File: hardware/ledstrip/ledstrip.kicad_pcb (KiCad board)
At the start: 4 copper layers, 107 x 107.5 mm, 126 parts, among them J1 Conn_ARM_JTAG_SWD_10, J2 USB_C_Receptacle_USB2.0_16P, J4 BMS connectors, J5 Ledstrip connector, J6 Header for STUSB4500 I2C, Q1 Q_NMOS, Q10 Q_PMOS, Q11 Q_NMOS, Q2 Q_NMOS, Q3 Q_NMOS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

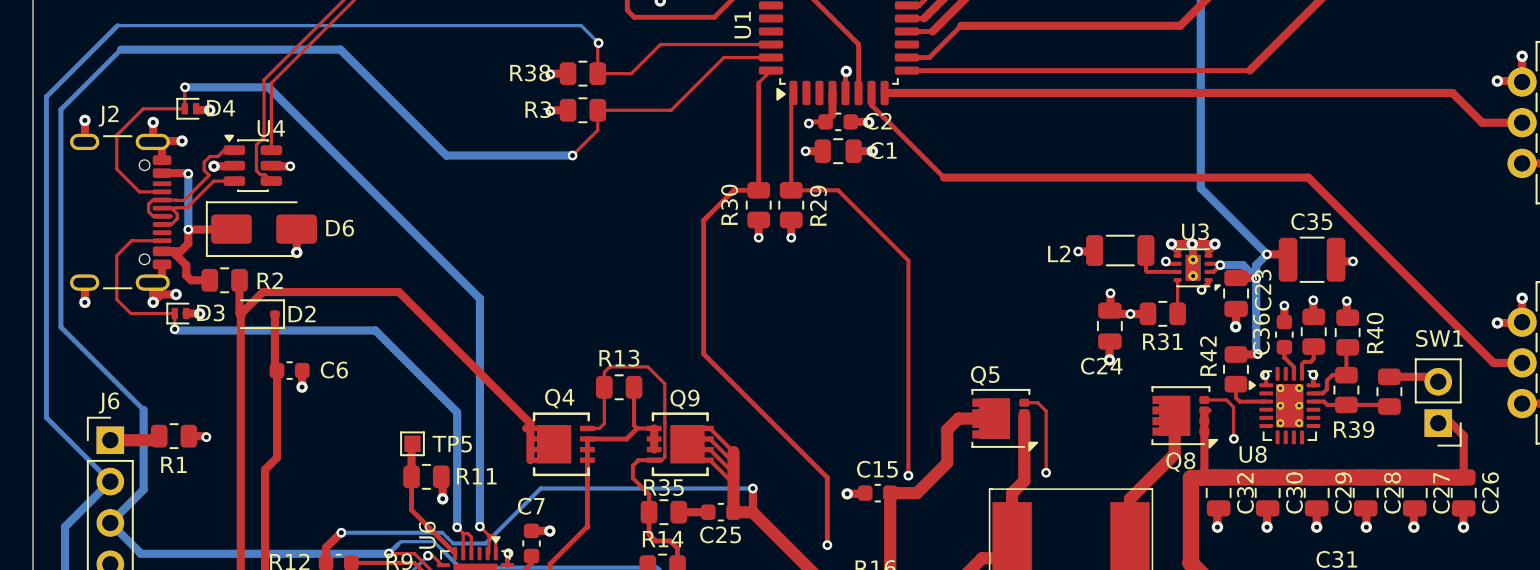
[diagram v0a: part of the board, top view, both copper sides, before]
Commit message: Fix ERC and DRC errors.
Use a custom copy of USB-C in project library to avoid having a version
mismatch with CI.
Fix QFN-20-1EP_3x4mm_P0.5mm_EP1.65x2.65mm_ThermalVias  mismatch pins.
Fix ERC errors.
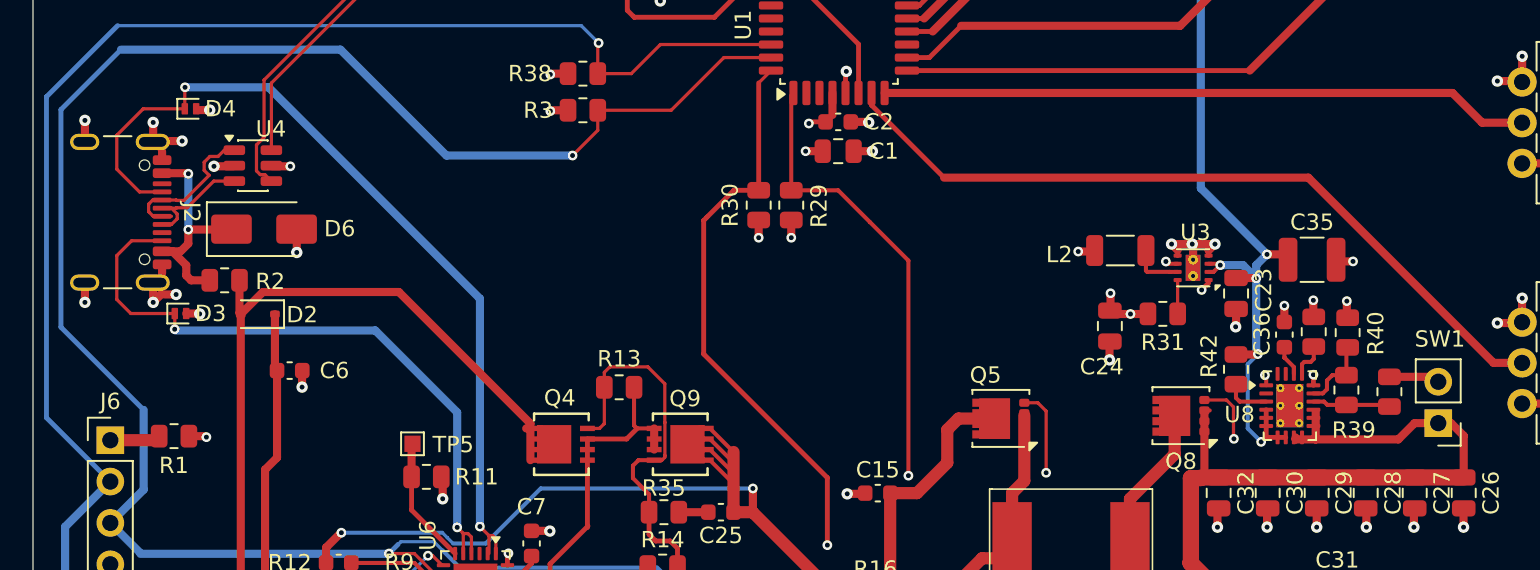
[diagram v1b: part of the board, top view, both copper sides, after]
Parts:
- J2: footprint Connector_USB:USB_C_Receptacle_GCT_USB4105-xx-A_16P_TopMnt_Horizontal -> ledstrip:USB_C_Receptacle_GCT_USB4105-xx-A_16P_TopMnt_Horizontal_PROJECT_COPY
- U8: footprint Package_DFN_QFN:QFN-20-1EP_3x4mm_P0.5mm_EP1.65x2.65mm_ThermalVias -> ledstrip:QFN-20-1EP_3x4mm_P0.5mm_EP1.65x2.65mm_ThermalVias_PROJECTCOPY
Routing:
- net /Battery Charger/BQ25703A_12V_OUT: track 56.8 -> 67.7 mm
- net +12V: track 64.1 -> 73.4 mm, vias 6 -> 7
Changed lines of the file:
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@@
 		)
 	)
-	(footprint "Package_DFN_QFN:QFN-20-1EP_3x4mm_P0.5mm_EP1.65x2.65mm_ThermalVias"
+	(footprint "ledstrip:QFN-20-1EP_3x4mm_P0.5mm_EP1.65x2.65mm_ThermalVias_PROJECTCOPY"
 		(layer "F.Cu")
 		(at 173.4352 111.6272)
@@
 		(tags "QFN NoLead")
 		(property "Reference" "U8"
-			(at -2.2646 3.0284 0)
+			(at -3.0852 0.5478 0)
 			(layer "F.SilkS")
 			(effects
@@
 			(pintype "unspecified")
 		)
-		(pad "4" smd roundrect
+		(pad "4_8" smd roundrect
 			(at -1.45 0.25)
 			(size 0.85 0.25)
 			(layers "F.Cu" "F.Mask" "F.Paste")
 			(roundrect_rratio 0.25)
+			(net 24 "+12V")
+			(pinfunction "OUT")
+			(pintype "unspecified")
 		)
-		(pad "5" smd roundrect
+		(pad "4_8" smd roundrect
 			(at -1.45 0.75)
 			(size 0.85 0.25)
 			(layers "F.Cu" "F.Mask" "F.Paste")
 			(roundrect_rratio 0.25)
+			(net 24 "+12V")
+			(pinfunction "OUT")
+			(pintype "unspecified")
 		)
-		(pad "6" smd roundrect
+		(pad "4_8" smd roundrect
 			(at -1.45 1.25)
 			(size 0.85 0.25)
 			(layers "F.Cu" "F.Mask" "F.Paste")
 			(roundrect_rratio 0.25)
+			(net 24 "+12V")
+			(pinfunction "OUT")
+			(pintype "unspecified")
 		)
-		(pad "7" smd roundrect
+		(pad "4_8" smd roundrect
 			(at -0.75 1.95)
 			(size 0.25 0.85)
 			(layers "F.Cu" "F.Mask" "F.Paste")
 			(roundrect_rratio 0.25)
+			(net 24 "+12V")
+			(pinfunction "OUT")
+			(pintype "unspecified")
 		)
-		(pad "8" smd roundrect
+		(pad "4_8" smd roundrect
 			(at -0.25 1.95)
 			(size 0.25 0.85)
 			(layers "F.Cu" "F.Mask" "F.Paste")
 			(roundrect_rratio 0.25)
+			(net 24 "+12V")
+			(pinfunction "OUT")
+			(pintype "unspecified")
 		)
-		(pad "9" smd roundrect
+		(pad "9_13" smd roundrect
 			(at 0.25 1.95)
 			(size 0.25 0.85)
 			(layers "F.Cu" "F.Mask" "F.Paste")
 			(roundrect_rratio 0.25)
+			(net 114 "/Battery Charger/BQ25703A_12V_OUT")
+			(pinfunction "IN")
+			(pintype "unspecified")
 		)
-		(pad "10" smd roundrect
+		(pad "9_13" smd roundrect
 			(at 0.75 1.95)
 			(size 0.25 0.85)
 			(layers "F.Cu" "F.Mask" "F.Paste")
 			(roundrect_rratio 0.25)
+			(net 114 "/Battery Charger/BQ25703A_12V_OUT")
+			(pinfunction "IN")
+			(pintype "unspecified")
 		)
-		(pad "11" smd roundrect
-			(at 1.45 1.25)
+		(pad "9_13" smd roundrect
+			(at 1.45 0.25)
 			(size 0.85 0.25)
 			(layers "F.Cu" "F.Mask" "F.Paste")
 			(roundrect_rratio 0.25)
+			(net 114 "/Battery Charger/BQ25703A_12V_OUT")
+			(pinfunction "IN")
+			(pintype "unspecified")
 		)
-		(pad "12" smd roundrect
+		(pad "9_13" smd roundrect
 			(at 1.45 0.75)
 			(size 0.85 0.25)
 			(layers "F.Cu" "F.Mask" "F.Paste")
 			(roundrect_rratio 0.25)
+			(net 114 "/Battery Charger/BQ25703A_12V_OUT")
+			(pinfunction "IN")
+			(pintype "unspecified")
 		)
-		(pad "13" smd roundrect
-			(at 1.45 0.25)
+		(pad "9_13" smd roundrect
+			(at 1.45 1.25)
 			(size 0.85 0.25)
 			(layers "F.Cu" "F.Mask" "F.Paste")
 			(roundrect_rratio 0.25)
+			(net 114 "/Battery Charger/BQ25703A_12V_OUT")
+			(pinfunction "IN")
+			(pintype "unspecified")
 		)
 		(pad "14" smd roundrect
@@
 			(pinfunction "PWRPAD")
 			(pintype "unspecified")
+			(zone_connect 2)
 		)
 		(embedded_fonts no)
@@
 		)
 	)
-	(footprint "Connector_USB:USB_C_Receptacle_GCT_USB4105-xx-A_16P_TopMnt_Horizontal"
+	(footprint "ledstrip:USB_C_Receptacle_GCT_USB4105-xx-A_16P_TopMnt_Horizontal_PROJECT_COPY"
 		(layer "F.Cu")
 		(at 100.5 99.75 -90)
@@
 		(tags "USB C Type-C Receptacle SMD USB 2.0 16P 16C USB4105-15-A USB4105-15-A-060 USB4105-15-A-120 USB4105-GF-A USB4105-GF-A-060 USB4105-GF-A-120")
 		(property "Reference" "J2"
-			(at -6 -0.5 0)
+			(at 0 -5.5 270)
 			(unlocked yes)
 			(layer "F.SilkS")
@@
 	)
 	(segment
+		(start 171.9478 113.5772)
+		(end 171.675 113.85)
+		(width 0.2)
+		(layer "F.Cu")
+		(net 24)
+	)
+	(segment
+		(start 171.9852 113.5398)
+		(end 171.9852 111.8772)
+		(width 0.3)
+		(layer "F.Cu")
+		(net 24)
+	)
+	(segment
 		(start 172.691 60.5)
 		(end 171 60.5)
@@
 	)
 	(segment
+		(start 171.9478 113.5772)
+		(end 171.9852 113.5398)
+		(width 0.2)
+		(layer "F.Cu")
+		(net 24)
+	)
+	(segment
 		(start 171.353 103.789)
 		(end 171.3738 103.8098)
@@
 	)
 	(segment
+		(start 173.1852 113.5772)
+		(end 171.9478 113.5772)
+		(width 0.3)
+		(layer "F.Cu")
+		(net 24)
+	)
+	(segment
 		(start 168.747 103.414)
 		(end 169.164 102.997)
@@
 	)
 	(via
+		(at 171.675 113.85)
+		(size 0.6)
+		(drill 0.3)
+		(layers "F.Cu" "B.Cu")
+		(net 24)
+	)
+	(via
 		(at 171.3738 103.8098)
 		(size 0.6)
@@
 	)
 	(segment
+		(start 171.675 113.85)
+		(end 170.85 113.025)
+		(width 0.25)
+		(layer "B.Cu")
+		(net 24)
+	)
+	(segment
 		(start 171.3738 103.8098)
 		(end 171.3738 102.997)
@@
 	)
 	(segment
+		(start 170.85 109.0834)
+		(end 171.4754 108.458)
+		(width 0.25)
+		(layer "B.Cu")
+		(net 24)
+	)
+	(segment
 		(start 172.0342 102.3366)
 		(end 167.9702 98.2726)
@@
 	)
 	(segment
+		(start 170.85 113.025)
+		(end 170.85 109.0834)
+		(width 0.25)
+		(layer "B.Cu")
+		(net 24)
+	)
+	(segment
 		(start 171.3738 103.8098)
 		(end 171.3738 108.3564)
@@
 	)
 	(segment
+		(start 181.1002 112.6998)
+		(end 180.1 113.7)
+		(width 0.5)
+		(layer "F.Cu")
+		(net 114)
+	)
+	(segment
+		(start 173.808 113.7)
+		(end 173.7862 113.6782)
+		(width 0.5)
+		(layer "F.Cu")
+		(net 114)
+	)
+	(segment
 		(start 184.116 113.4786)
 		(end 184.116 116.036)
@@
 	)
 	(segment
+		(start 180.1 113.7)
+		(end 175.025 113.7)
+		(width 0.5)
+		(layer "F.Cu")
+		(net 114)
+	)
+	(segment
 		(start 173.228 124.206)
 		(end 170.2562 124.206)
@@
 	)
 	(segment
+		(start 182.5498 112.6998)
+		(end 181.1002 112.6998)
+		(width 0.5)
+		(layer "F.Cu")
+		(net 114)
+	)
+	(segment
 		(start 168.0122 116.036)
 		(end 184.116 116.036)
@@
 	)
 	(segment
+		(start 175.025 113.7)
+		(end 175.025 112.017)
+		(width 0.5)
+		(layer "F.Cu")
+		(net 114)
+	)
+	(segment
 		(start 172.085 116.027)
 		(end 172.076 116.036)
@@
 	)
 	(segment
+		(start 175.025 113.7)
+		(end 173.808 113.7)
+		(width 0.5)
+		(layer "F.Cu")
+		(net 114)
+	)
+	(segment
 		(start 169.037 116.007)
 		(end 169.066 116.036)
@@
 		(width 0.5)
 		(layer "F.Cu")
+		(net 114)
+	)
+	(segment
+		(start 173.7862 113.6782)
+		(end 173.7862 113.5772)
+		(width 0.5)
+		(layer "F.Cu")

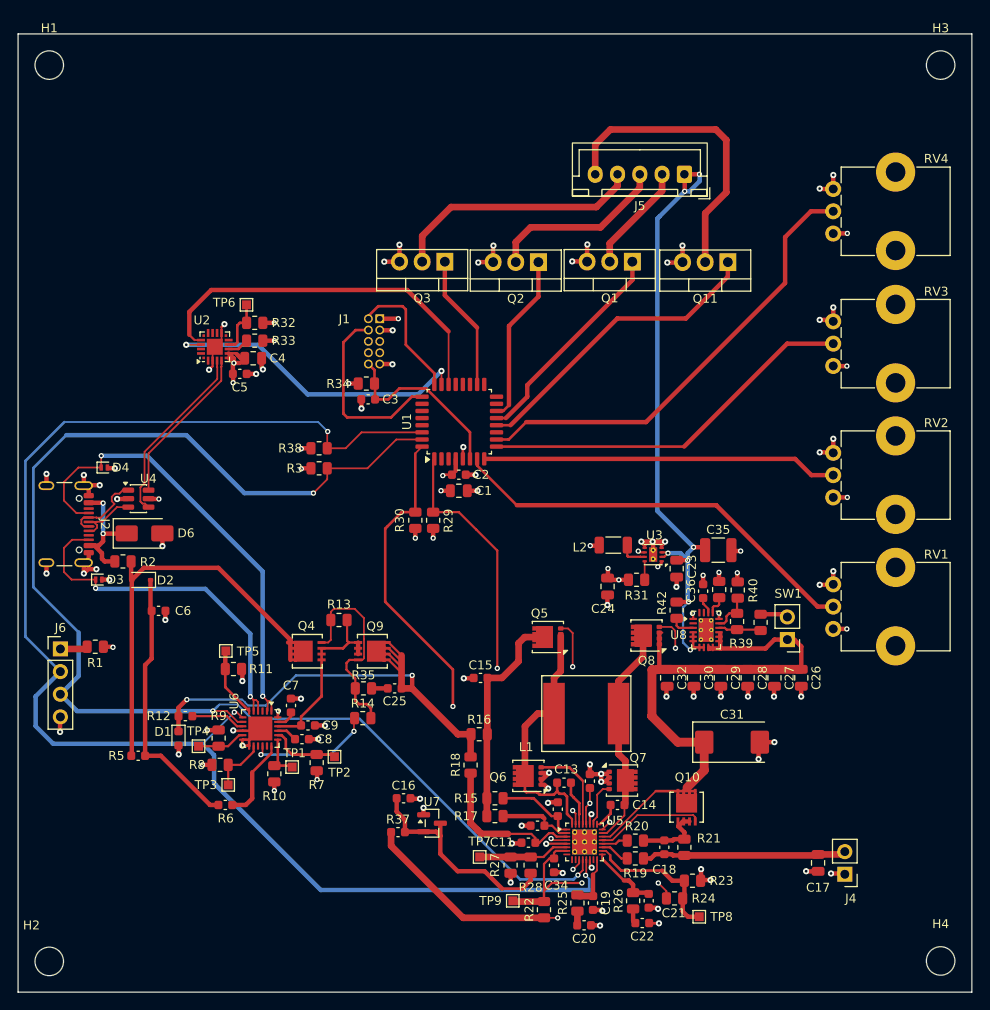
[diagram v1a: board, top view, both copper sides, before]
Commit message: Add a lot of TestPoints
Move P-FET at the edge of board.
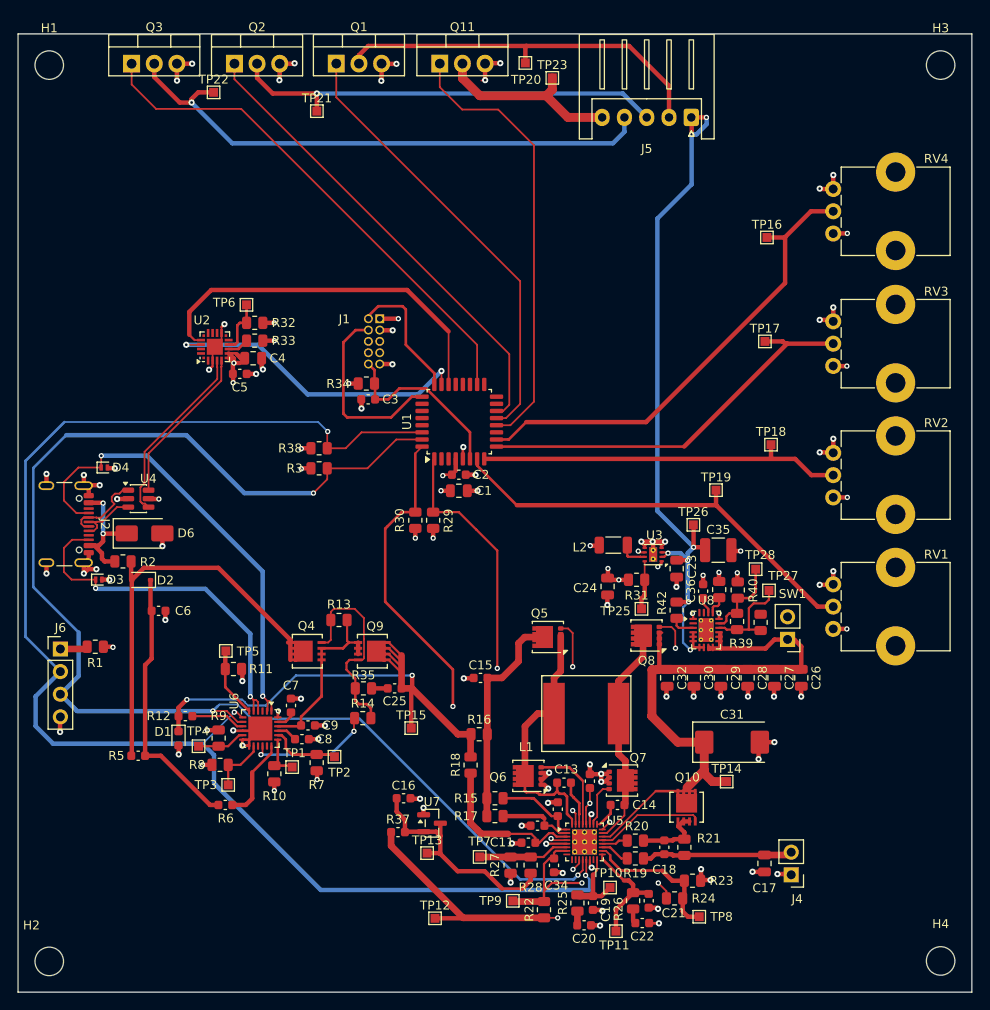
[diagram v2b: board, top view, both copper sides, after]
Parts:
- added TP10: TestPoint, TestPoint:TestPoint_Pad_1.0x1.0mm, F.Cu at (162.7, 140.5)
- added TP11: TestPoint, TestPoint:TestPoint_Pad_1.0x1.0mm, F.Cu at (163.3, 145.4)
- added TP12: TestPoint, TestPoint:TestPoint_Pad_1.0x1.0mm, F.Cu at (143.0, 144.0)
- added TP13: TestPoint, TestPoint:TestPoint_Pad_1.0x1.0mm, F.Cu at (142.1, 136.7)
- added TP14: TestPoint, TestPoint:TestPoint_Pad_1.0x1.0mm, F.Cu at (175.7, 128.6)
- added TP15: TestPoint, TestPoint:TestPoint_Pad_1.0x1.0mm, F.Cu at (140.4, 122.6)
- added TP16: TestPoint, TestPoint:TestPoint_Pad_1.0x1.0mm, F.Cu at (180.3, 67.6)
- added TP17: TestPoint, TestPoint:TestPoint_Pad_1.0x1.0mm, F.Cu at (180.0, 79.2)
- added TP18: TestPoint, TestPoint:TestPoint_Pad_1.0x1.0mm, F.Cu at (180.7, 90.8)
- added TP19: TestPoint, TestPoint:TestPoint_Pad_1.0x1.0mm, F.Cu at (174.5, 95.9)
- added TP20: TestPoint, TestPoint:TestPoint_Pad_1.0x1.0mm, F.Cu at (153.2, 48.0)
- added TP21: TestPoint, TestPoint:TestPoint_Pad_1.0x1.0mm, F.Cu at (129.8, 53.4)
- added TP22: TestPoint, TestPoint:TestPoint_Pad_1.0x1.0mm, F.Cu at (118.2, 51.3)
- added TP23: TestPoint, TestPoint:TestPoint_Pad_1.0x1.0mm, F.Cu at (156.2, 49.7)
- added TP25: TestPoint, TestPoint:TestPoint_Pad_1.0x1.0mm, F.Cu at (166.2, 109.2)
- added TP26: TestPoint, TestPoint:TestPoint_Pad_1.0x1.0mm, F.Cu at (172.0, 99.8)
- added TP27: TestPoint, TestPoint:TestPoint_Pad_1.0x1.0mm, F.Cu at (180.5, 107.2)
- added TP28: TestPoint, TestPoint:TestPoint_Pad_1.0x1.0mm, F.Cu at (179.0, 104.8)
- J5: footprint Connector_JST:JST_XH_B5B-XH-A_1x05_P2.50mm_Vertical -> Connector_JST:JST_XH_S5B-XH-A_1x05_P2.50mm_Horizontal
- moved Q3 41.6 mm to (109.0, 48.1), turned to 0 degrees
- moved Q2 40.7 mm to (120.5, 48.1), turned to 0 degrees
- moved Q1 40.0 mm to (132.0, 48.1), turned to 0 degrees
- moved Q11 39.2 mm to (143.6, 48.1), turned to 0 degrees
- moved J5 6.43 mm to (171.8, 54.1)
- moved C17 6.01 mm to (180.0, 137.8)
- moved J4 6.01 mm to (183.0, 139.1)
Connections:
- R4 pad 2: Net-(SW1-B) -> Net-(R4-Pad2)
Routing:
- net /leds/PWM_B: track 15.3 -> 57.6 mm
- net /leds/LED_B: track 28.4 -> 62.7 mm, vias 0 -> 1
- net /leds/PWM_G: track 19.1 -> 52.8 mm
- net /leds/LED_R: track 12.2 -> 43.5 mm
- net /leds/LED_G: track 20.2 -> 49.1 mm, vias 0 -> 1
- net /leds/PWM_R: track 24.5 -> 50.0 mm
- net /leds/PWM_W: track 34.5 -> 50.0 mm
- net /leds/LED_W: track 33.9 -> 21.4 mm
- net +12V: track 73.4 -> 82.6 mm
- net Net-(U8-EN_UVLO): track 4.79 -> 10.9 mm
- net /Battery Charger/BMS_P+: track 23.0 -> 17.1 mm
- net Net-(U8-OVP): track 4.54 -> 9.67 mm
- net /Battery Charger/BQ25703A_COMP2: track 7.94 -> 13.1 mm
- net /Battery Charger/V_SNK: track 56.8 -> 61.3 mm
- net TPS62162_PG: track 2.08 -> 5.48 mm
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
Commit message: Resolv DRC warnings.
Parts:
- moved J5 0.05 mm to (171.8, 54.2)
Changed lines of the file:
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@@
 	(footprint "TOT-220-3:TO-220-3_Vertical"
 		(layer "F.Cu")
-		(at 108.9914 48.0924)
+		(at 108.9914 48.1178)
 		(descr "TO-220-3, Vertical, RM 2.54mm, see https://www.vishay.com/docs/66542/to-220-1.pdf, generated with kicad-footprint-generator TO_SOT_THT_generate.py")
 		(tags "TO-220-3 Vertical RM 2.54mm")
@@
 		(tags "QFN NoLead")
 		(property "Reference" "U8"
-			(at 0 -3.33 0)
+			(at -3.1282 0.5138 0)
 			(layer "F.SilkS")
 			(effects
@@
 	(footprint "TOT-220-3:TO-220-3_Vertical"
 		(layer "F.Cu")
-		(at 120.523 48.0924)
+		(at 120.5484 48.1178)
 		(descr "TO-220-3, Vertical, RM 2.54mm, see https://www.vishay.com/docs/66542/to-220-1.pdf, generated with kicad-footprint-generator TO_SOT_THT_generate.py")
 		(tags "TO-220-3 Vertical RM 2.54mm")
@@
 		(tags "test point SMD pad rectangle square")
 		(property "Reference" "TP14"
-			(at 0 -1.448 0)
+			(at 2.9972 0 0)
 			(layer "F.SilkS")
 			(effects
@@
 	(footprint "TOT-220-3:TO-220-3_Vertical"
 		(layer "F.Cu")
-		(at 143.5608 48.0822)
+		(at 143.5608 48.1178)
 		(descr "TO-220-3, Vertical, RM 2.54mm, see https://www.vishay.com/docs/66542/to-220-1.pdf, generated with kicad-footprint-generator TO_SOT_THT_generate.py")
 		(tags "TO-220-3 Vertical RM 2.54mm")
@@
 	(footprint "Connector_JST:JST_XH_S5B-XH-A_1x05_P2.50mm_Horizontal"
 		(layer "F.Cu")
-		(at 171.7764 54.118 180)
+		(at 171.7764 54.1688 180)
 		(descr "JST XH series connector, S5B-XH-A (http://www.jst-mfg.com/product/pdf/eng/eXH.pdf), generated with kicad-footprint-generator")
 		(tags "connector JST XH horizontal")
@@
 		(tags "test point SMD pad rectangle square")
 		(property "Reference" "TP13"
-			(at 0 -1.448 0)
+			(at -2.921 0.0508 0)
 			(layer "F.SilkS")
 			(effects
@@
 	(footprint "TOT-220-3:TO-220-3_Vertical"
 		(layer "F.Cu")
-		(at 131.953 48.0822)
+		(at 131.953 48.1178)
 		(descr "TO-220-3, Vertical, RM 2.54mm, see https://www.vishay.com/docs/66542/to-220-1.pdf, generated with kicad-footprint-generator TO_SOT_THT_generate.py")
 		(tags "TO-220-3 Vertical RM 2.54mm")
@@
 		(tags "test point SMD pad rectangle square")
 		(property "Reference" "TP22"
-			(at 0 -1.448 0)
+			(at 2.9718 0 0)
 			(layer "F.SilkS")
 			(effects

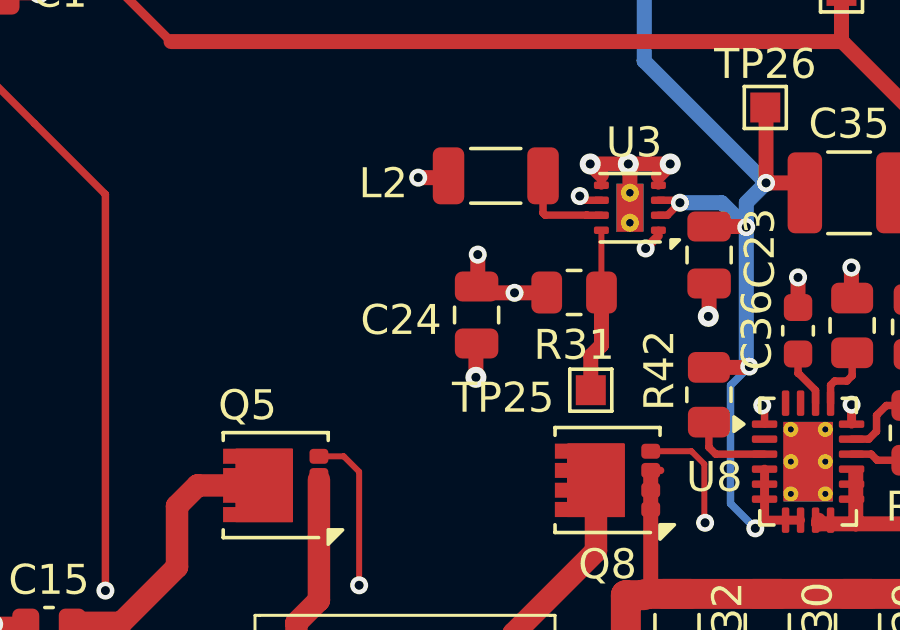
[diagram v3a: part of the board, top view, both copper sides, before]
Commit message: Mark through-hole component "Do not place" in schematics.
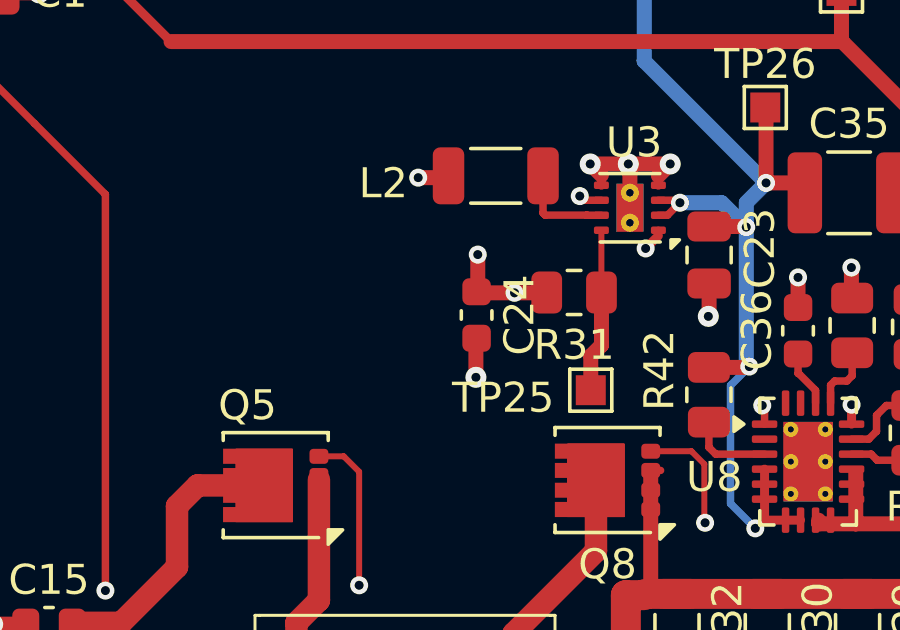
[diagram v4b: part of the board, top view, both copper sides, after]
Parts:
- C24: footprint Capacitor_SMD:C_0805_2012Metric -> Capacitor_SMD:C_0603_1608Metric
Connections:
- R4 pad 2: Net-(R4-Pad2) -> Net-(SW1-B)
